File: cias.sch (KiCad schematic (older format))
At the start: 63 parts, among them CN13 KEYBOARD, CN6 SERIAL_DB25M, CN7 PARALLEL_DB25F, Q501 2N3904, Q502 2N3906, Q503 2N3906, Q711 2N3904, U38 MC1488, U39 MC1489, U42 NE555, U7 VIA_8520, U8 VIA_8520

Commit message: Add EMI filter types
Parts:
- E501, E502, E503: EMI_FILTER_TYPE (none) -> R
- E511, E512, E513, E514, E515, E516, E517, E518, E519, E521, E522, E523, E524, E631, E632: EMI_FILTER_TYPE (none) -> NORMAL
- E520, E531, E532, E533, E534, E535, E536, E537, E538: EMI_FILTER_TYPE (none) -> W/FERRITE
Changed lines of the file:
@@
 F 3 "http://www.murata.com/~/media/webrenewal/support/library/catalog/products/emc/emifil/c31e.ashx?la=en-gb" V 9950 1990 50  0001 C CNN
 F 4 "PARALLEL" H 9950 1990 50  0001 C CNN "Optional"
+F 5 "W/FERRITE" H 9950 1990 50  0001 C CNN "EMI_FILTER_TYPE"
 	1    9950 1990
 	-1   0    0    -1
@@
 F 3 "http://www.murata.com/~/media/webrenewal/support/library/catalog/products/emc/emifil/c31e.ashx?la=en-gb" V 8045 1490 50  0001 C CNN
 F 4 "PARALLEL" H 8045 1490 50  0001 C CNN "Optional"
+F 5 "NORMAL" H 8045 1490 50  0001 C CNN "EMI_FILTER_TYPE"
 	1    8045 1490
 	1    0    0    -1
@@
 F 3 "http://www.murata.com/~/media/webrenewal/support/library/catalog/products/emc/emifil/c31e.ashx?la=en-gb" V 8430 1690 50  0001 C CNN
 F 4 "PARALLEL" H 8430 1690 50  0001 C CNN "Optional"
+F 5 "NORMAL" H 8430 1690 50  0001 C CNN "EMI_FILTER_TYPE"
 	1    8430 1690
 	1    0    0    -1
@@
 F 3 "http://www.murata.com/~/media/webrenewal/support/library/catalog/products/emc/emifil/c31e.ashx?la=en-gb" V 8045 1890 50  0001 C CNN
 F 4 "PARALLEL" H 8045 1890 50  0001 C CNN "Optional"
+F 5 "NORMAL" H 8045 1890 50  0001 C CNN "EMI_FILTER_TYPE"
 	1    8045 1890
 	1    0    0    -1
@@
 F 3 "http://www.murata.com/~/media/webrenewal/support/library/catalog/products/emc/emifil/c31e.ashx?la=en-gb" V 8430 2090 50  0001 C CNN
 F 4 "PARALLEL" H 8430 2090 50  0001 C CNN "Optional"
+F 5 "NORMAL" H 8430 2090 50  0001 C CNN "EMI_FILTER_TYPE"
 	1    8430 2090
 	1    0    0    -1
@@
 F 3 "http://www.murata.com/~/media/webrenewal/support/library/catalog/products/emc/emifil/c31e.ashx?la=en-gb" V 8045 2290 50  0001 C CNN
 F 4 "PARALLEL" H 8045 2290 50  0001 C CNN "Optional"
+F 5 "NORMAL" H 8045 2290 50  0001 C CNN "EMI_FILTER_TYPE"
 	1    8045 2290
 	1    0    0    -1
@@
 F 3 "http://www.murata.com/~/media/webrenewal/support/library/catalog/products/emc/emifil/c31e.ashx?la=en-gb" V 8430 2490 50  0001 C CNN
 F 4 "PARALLEL" H 8430 2490 50  0001 C CNN "Optional"
+F 5 "NORMAL" H 8430 2490 50  0001 C CNN "EMI_FILTER_TYPE"
 	1    8430 2490
 	1    0    0    -1
@@
 F 3 "http://www.murata.com/~/media/webrenewal/support/library/catalog/products/emc/emifil/c31e.ashx?la=en-gb" V 8045 2690 50  0001 C CNN
 F 4 "PARALLEL" H 8045 2690 50  0001 C CNN "Optional"
+F 5 "NORMAL" H 8045 2690 50  0001 C CNN "EMI_FILTER_TYPE"
 	1    8045 2690
 	1    0    0    -1
@@
 F 3 "http://www.murata.com/~/media/webrenewal/support/library/catalog/products/emc/emifil/c31e.ashx?la=en-gb" V 8430 2890 50  0001 C CNN
 F 4 "PARALLEL" H 8430 2890 50  0001 C CNN "Optional"
+F 5 "NORMAL" H 8430 2890 50  0001 C CNN "EMI_FILTER_TYPE"
 	1    8430 2890
 	1    0    0    -1
@@
 F 3 "http://www.murata.com/~/media/webrenewal/support/library/catalog/products/emc/emifil/c31e.ashx?la=en-gb" V 8045 3090 50  0001 C CNN
 F 4 "PARALLEL" H 8045 3090 50  0001 C CNN "Optional"
+F 5 "NORMAL" H 8045 3090 50  0001 C CNN "EMI_FILTER_TYPE"
 	1    8045 3090
 	1    0    0    -1
@@
 F 3 "http://www.murata.com/~/media/webrenewal/support/library/catalog/products/emc/emifil/c31e.ashx?la=en-gb" V 8430 3290 50  0001 C CNN
 F 4 "PARALLEL" H 8430 3290 50  0001 C CNN "Optional"
+F 5 "NORMAL" H 8430 3290 50  0001 C CNN "EMI_FILTER_TYPE"
 	1    8430 3290
 	1    0    0    -1
@@
 F 3 "http://www.murata.com/~/media/webrenewal/support/library/catalog/products/emc/emifil/c31e.ashx?la=en-gb" V 8045 3490 50  0001 C CNN
 F 4 "PARALLEL" H 8045 3490 50  0001 C CNN "Optional"
+F 5 "NORMAL" H 8045 3490 50  0001 C CNN "EMI_FILTER_TYPE"
 	1    8045 3490
 	1    0    0    -1
@@
 F 3 "http://www.murata.com/~/media/webrenewal/support/library/catalog/products/emc/emifil/c31e.ashx?la=en-gb" V 8430 3690 50  0001 C CNN
 F 4 "PARALLEL" H 8430 3690 50  0001 C CNN "Optional"
+F 5 "NORMAL" H 8430 3690 50  0001 C CNN "EMI_FILTER_TYPE"
 	1    8430 3690
 	1    0    0    -1
@@
 F 3 "http://www.murata.com/~/media/webrenewal/support/library/catalog/products/emc/emifil/c31e.ashx?la=en-gb" V 8045 3890 50  0001 C CNN
 F 4 "PARALLEL" H 8045 3890 50  0001 C CNN "Optional"
+F 5 "NORMAL" H 8045 3890 50  0001 C CNN "EMI_FILTER_TYPE"
 	1    8045 3890
 	1    0    0    -1
@@
 F 3 "http://www.murata.com/~/media/webrenewal/support/library/catalog/products/emc/emifil/c31e.ashx?la=en-gb" V 8045 6710 50  0001 C CNN
 F 4 "SERIAL" H 8045 6710 50  0001 C CNN "Optional"
+F 5 "W/FERRITE" H 8045 6710 50  0001 C CNN "EMI_FILTER_TYPE"
 	1    8045 6710
 	1    0    0    -1
@@
 F 3 "http://www.murata.com/~/media/webrenewal/support/library/catalog/products/emc/emifil/c31e.ashx?la=en-gb" V 8430 6910 50  0001 C CNN
 F 4 "SERIAL" H 8430 6910 50  0001 C CNN "Optional"
+F 5 "W/FERRITE" H 8430 6910 50  0001 C CNN "EMI_FILTER_TYPE"
 	1    8430 6910
 	1    0    0    -1
@@
 F 3 "http://www.murata.com/~/media/webrenewal/support/library/catalog/products/emc/emifil/c31e.ashx?la=en-gb" V 8045 7110 50  0001 C CNN
 F 4 "SERIAL" H 8045 7110 50  0001 C CNN "Optional"
+F 5 "W/FERRITE" H 8045 7110 50  0001 C CNN "EMI_FILTER_TYPE"
 	1    8045 7110
 	1    0    0    -1
@@
 F 3 "http://www.murata.com/~/media/webrenewal/support/library/catalog/products/emc/emifil/c31e.ashx?la=en-gb" V 8430 7310 50  0001 C CNN
 F 4 "SERIAL" H 8430 7310 50  0001 C CNN "Optional"
+F 5 "W/FERRITE" H 8430 7310 50  0001 C CNN "EMI_FILTER_TYPE"
 	1    8430 7310
 	1    0    0    -1
@@
 F 3 "http://www.murata.com/~/media/webrenewal/support/library/catalog/products/emc/emifil/c31e.ashx?la=en-gb" V 8045 7910 50  0001 C CNN
 F 4 "SERIAL" H 8045 7910 50  0001 C CNN "Optional"
+F 5 "W/FERRITE" H 8045 7910 50  0001 C CNN "EMI_FILTER_TYPE"
 	1    8045 7910
 	1    0    0    -1
@@
 F 3 "http://www.murata.com/~/media/webrenewal/support/library/catalog/products/emc/emifil/c31e.ashx?la=en-gb" V 10180 7810 50  0001 C CNN
 F 4 "SERIAL" H 10180 7810 50  0001 C CNN "Optional"
+F 5 "W/FERRITE" H 10180 7810 50  0001 C CNN "EMI_FILTER_TYPE"
 	1    10180 7810
 	-1   0    0    -1
@@
 F 3 "http://www.murata.com/~/media/webrenewal/support/library/catalog/products/emc/emifil/c31e.ashx?la=en-gb" V 10180 8210 50  0001 C CNN
 F 4 "SERIAL" H 10180 8210 50  0001 C CNN "Optional"
+F 5 "W/FERRITE" H 10180 8210 50  0001 C CNN "EMI_FILTER_TYPE"
 	1    10180 8210
 	-1   0    0    -1
@@
 F 3 "http://www.murata.com/~/media/webrenewal/support/library/catalog/products/emc/emifil/c31e.ashx?la=en-gb" V 14545 4085 50  0001 C CNN
 F 4 "KEYBOARD" H 14545 4085 50  0001 C CNN "Optional"
+F 5 "NORMAL" H 14545 4085 50  0001 C CNN "EMI_FILTER_TYPE"
 	1    14545 4085
 	1    0    0    -1
@@
 F 3 "http://www.murata.com/~/media/webrenewal/support/library/catalog/products/emc/emifil/c31e.ashx?la=en-gb" V 14545 4440 50  0001 C CNN
 F 4 "KEYBOARD" H 14545 4440 50  0001 C CNN "Optional"
+F 5 "NORMAL" H 14545 4440 50  0001 C CNN "EMI_FILTER_TYPE"
 	1    14545 4440
 	1    0    0    -1
@@
 F 3 "http://www.murata.com/~/media/webrenewal/support/library/catalog/products/emc/emifil/c31e.ashx?la=en-gb" V 8045 7510 50  0001 C CNN
 F 4 "SERIAL" H 8045 7510 50  0001 C CNN "Optional"
+F 5 "W/FERRITE" H 8045 7510 50  0001 C CNN "EMI_FILTER_TYPE"
 	1    8045 7510
 	1    0    0    -1
@@
 F 3 "http://www.murata.com/~/media/webrenewal/support/library/catalog/products/emc/emifil/c31e.ashx?la=en-gb" V 8430 8110 50  0001 C CNN
 F 4 "SERIAL" H 8430 8110 50  0001 C CNN "Optional"
+F 5 "R" H 8430 8110 50  0001 C CNN "EMI_FILTER_TYPE"
 	1    8430 8110
 	1    0    0    -1
@@
 F 3 "http://www.murata.com/~/media/webrenewal/support/library/catalog/products/emc/emifil/c31e.ashx?la=en-gb" V 8045 8310 50  0001 C CNN
 F 4 "SERIAL" H 8045 8310 50  0001 C CNN "Optional"
+F 5 "R" H 8045 8310 50  0001 C CNN "EMI_FILTER_TYPE"
 	1    8045 8310
 	1    0    0    -1
@@
 F 3 "http://www.murata.com/~/media/webrenewal/support/library/catalog/products/emc/emifil/c31e.ashx?la=en-gb" V 10105 1590 50  0001 C CNN
 F 4 "PARALLEL" H 10105 1590 50  0001 C CNN "Optional"
+F 5 "R" H 10105 1590 50  0001 C CNN "EMI_FILTER_TYPE"
 	1    10105 1590
 	-1   0    0    -1

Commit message: Add part numbers for EMI filters Not the original filters, but what seem to be suitable replacements available today
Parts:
- E511, E512, E513, E514, E515, E516, E517, E518, E519, E521, E522, E523, E524, E631, E632: Cost (none) -> 0.233; MFG Part Num (none) -> DSS1NB32A101Q91A (has ferrite)
- E520, E531, E533, E535, E536, E537, E538: Cost (none) -> 0.233; MFG Name (none) -> MURATA; MFG Part Num (none) -> DSS1NB32A471Q91A
- E532, E534: Cost (none) -> 0.238; MFG Name (none) -> MURATA; MFG Part Num (none) -> DSS1NB32A151Q91A
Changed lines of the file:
@@
 F 4 "PARALLEL" H 9950 1990 50  0001 C CNN "Optional"
 F 5 "W/FERRITE" H 9950 1990 50  0001 C CNN "EMI_FILTER_TYPE"
+F 6 "0.233" H 9950 1990 50  0001 C CNN "Cost"
+F 7 "MURATA" H 9950 1990 50  0001 C CNN "MFG Name"
+F 8 "DSS1NB32A471Q91A" H 9950 1990 50  0001 C CNN "MFG Part Num"
 	1    9950 1990
 	-1   0    0    -1
@@
 F 4 "PARALLEL" H 8045 1490 50  0001 C CNN "Optional"
 F 5 "NORMAL" H 8045 1490 50  0001 C CNN "EMI_FILTER_TYPE"
+F 6 "0.233" H 8045 1490 50  0001 C CNN "Cost"
+F 7 "DSS1NB32A101Q91A (has ferrite)" H 8045 1490 50  0001 C CNN "MFG Part Num"
 	1    8045 1490
 	1    0    0    -1
@@
 F 4 "PARALLEL" H 8430 1690 50  0001 C CNN "Optional"
 F 5 "NORMAL" H 8430 1690 50  0001 C CNN "EMI_FILTER_TYPE"
+F 6 "0.233" H 8430 1690 50  0001 C CNN "Cost"
+F 7 "DSS1NB32A101Q91A (has ferrite)" H 8430 1690 50  0001 C CNN "MFG Part Num"
 	1    8430 1690
 	1    0    0    -1
@@
 F 4 "PARALLEL" H 8045 1890 50  0001 C CNN "Optional"
 F 5 "NORMAL" H 8045 1890 50  0001 C CNN "EMI_FILTER_TYPE"
+F 6 "0.233" H 8045 1890 50  0001 C CNN "Cost"
+F 7 "DSS1NB32A101Q91A (has ferrite)" H 8045 1890 50  0001 C CNN "MFG Part Num"
 	1    8045 1890
 	1    0    0    -1
@@
 F 4 "PARALLEL" H 8430 2090 50  0001 C CNN "Optional"
 F 5 "NORMAL" H 8430 2090 50  0001 C CNN "EMI_FILTER_TYPE"
+F 6 "0.233" H 8430 2090 50  0001 C CNN "Cost"
+F 7 "DSS1NB32A101Q91A (has ferrite)" H 8430 2090 50  0001 C CNN "MFG Part Num"
 	1    8430 2090
 	1    0    0    -1
@@
 F 4 "PARALLEL" H 8045 2290 50  0001 C CNN "Optional"
 F 5 "NORMAL" H 8045 2290 50  0001 C CNN "EMI_FILTER_TYPE"
+F 6 "0.233" H 8045 2290 50  0001 C CNN "Cost"
+F 7 "DSS1NB32A101Q91A (has ferrite)" H 8045 2290 50  0001 C CNN "MFG Part Num"
 	1    8045 2290
 	1    0    0    -1
@@
 F 4 "PARALLEL" H 8430 2490 50  0001 C CNN "Optional"
 F 5 "NORMAL" H 8430 2490 50  0001 C CNN "EMI_FILTER_TYPE"
+F 6 "0.233" H 8430 2490 50  0001 C CNN "Cost"
+F 7 "DSS1NB32A101Q91A (has ferrite)" H 8430 2490 50  0001 C CNN "MFG Part Num"
 	1    8430 2490
 	1    0    0    -1
@@
 F 4 "PARALLEL" H 8045 2690 50  0001 C CNN "Optional"
 F 5 "NORMAL" H 8045 2690 50  0001 C CNN "EMI_FILTER_TYPE"
+F 6 "0.233" H 8045 2690 50  0001 C CNN "Cost"
+F 7 "DSS1NB32A101Q91A (has ferrite)" H 8045 2690 50  0001 C CNN "MFG Part Num"
 	1    8045 2690
 	1    0    0    -1
@@
 F 4 "PARALLEL" H 8430 2890 50  0001 C CNN "Optional"
 F 5 "NORMAL" H 8430 2890 50  0001 C CNN "EMI_FILTER_TYPE"
+F 6 "0.233" H 8430 2890 50  0001 C CNN "Cost"
+F 7 "DSS1NB32A101Q91A (has ferrite)" H 8430 2890 50  0001 C CNN "MFG Part Num"
 	1    8430 2890
 	1    0    0    -1
@@
 F 4 "PARALLEL" H 8045 3090 50  0001 C CNN "Optional"
 F 5 "NORMAL" H 8045 3090 50  0001 C CNN "EMI_FILTER_TYPE"
+F 6 "0.233" H 8045 3090 50  0001 C CNN "Cost"
+F 7 "DSS1NB32A101Q91A (has ferrite)" H 8045 3090 50  0001 C CNN "MFG Part Num"
 	1    8045 3090
 	1    0    0    -1
@@
 F 4 "PARALLEL" H 8430 3290 50  0001 C CNN "Optional"
 F 5 "NORMAL" H 8430 3290 50  0001 C CNN "EMI_FILTER_TYPE"
+F 6 "0.233" H 8430 3290 50  0001 C CNN "Cost"
+F 7 "DSS1NB32A101Q91A (has ferrite)" H 8430 3290 50  0001 C CNN "MFG Part Num"
 	1    8430 3290
 	1    0    0    -1
@@
 F 4 "PARALLEL" H 8045 3490 50  0001 C CNN "Optional"
 F 5 "NORMAL" H 8045 3490 50  0001 C CNN "EMI_FILTER_TYPE"
+F 6 "0.233" H 8045 3490 50  0001 C CNN "Cost"
+F 7 "DSS1NB32A101Q91A (has ferrite)" H 8045 3490 50  0001 C CNN "MFG Part Num"
 	1    8045 3490
 	1    0    0    -1
@@
 F 4 "PARALLEL" H 8430 3690 50  0001 C CNN "Optional"
 F 5 "NORMAL" H 8430 3690 50  0001 C CNN "EMI_FILTER_TYPE"
+F 6 "0.233" H 8430 3690 50  0001 C CNN "Cost"
+F 7 "DSS1NB32A101Q91A (has ferrite)" H 8430 3690 50  0001 C CNN "MFG Part Num"
 	1    8430 3690
 	1    0    0    -1
@@
 F 4 "PARALLEL" H 8045 3890 50  0001 C CNN "Optional"
 F 5 "NORMAL" H 8045 3890 50  0001 C CNN "EMI_FILTER_TYPE"
+F 6 "0.233" H 8045 3890 50  0001 C CNN "Cost"
+F 7 "DSS1NB32A101Q91A (has ferrite)" H 8045 3890 50  0001 C CNN "MFG Part Num"
 	1    8045 3890
 	1    0    0    -1
@@
 F 4 "SERIAL" H 8045 6710 50  0001 C CNN "Optional"
 F 5 "W/FERRITE" H 8045 6710 50  0001 C CNN "EMI_FILTER_TYPE"
+F 6 "0.238" H 8045 6710 50  0001 C CNN "Cost"
+F 7 "MURATA" H 8045 6710 50  0001 C CNN "MFG Name"
+F 8 "DSS1NB32A151Q91A " H 8045 6710 50  0001 C CNN "MFG Part Num"
 	1    8045 6710
 	1    0    0    -1
@@
 F 4 "SERIAL" H 8430 6910 50  0001 C CNN "Optional"
 F 5 "W/FERRITE" H 8430 6910 50  0001 C CNN "EMI_FILTER_TYPE"
+F 6 "0.238" H 8430 6910 50  0001 C CNN "Cost"
+F 7 "MURATA" H 8430 6910 50  0001 C CNN "MFG Name"
+F 8 "DSS1NB32A151Q91A " H 8430 6910 50  0001 C CNN "MFG Part Num"
 	1    8430 6910
 	1    0    0    -1
@@
 F 4 "SERIAL" H 8045 7110 50  0001 C CNN "Optional"
 F 5 "W/FERRITE" H 8045 7110 50  0001 C CNN "EMI_FILTER_TYPE"
+F 6 "0.233" H 8045 7110 50  0001 C CNN "Cost"
+F 7 "MURATA" H 8045 7110 50  0001 C CNN "MFG Name"
+F 8 "DSS1NB32A471Q91A" H 8045 7110 50  0001 C CNN "MFG Part Num"
 	1    8045 7110
 	1    0    0    -1
@@
 F 4 "SERIAL" H 8430 7310 50  0001 C CNN "Optional"
 F 5 "W/FERRITE" H 8430 7310 50  0001 C CNN "EMI_FILTER_TYPE"
+F 6 "0.233" H 8430 7310 50  0001 C CNN "Cost"
+F 7 "MURATA" H 8430 7310 50  0001 C CNN "MFG Name"
+F 8 "DSS1NB32A471Q91A" H 8430 7310 50  0001 C CNN "MFG Part Num"
 	1    8430 7310
 	1    0    0    -1
@@
 F 4 "SERIAL" H 8045 7910 50  0001 C CNN "Optional"
 F 5 "W/FERRITE" H 8045 7910 50  0001 C CNN "EMI_FILTER_TYPE"
+F 6 "0.233" H 8045 7910 50  0001 C CNN "Cost"
+F 7 "MURATA" H 8045 7910 50  0001 C CNN "MFG Name"
+F 8 "DSS1NB32A471Q91A" H 8045 7910 50  0001 C CNN "MFG Part Num"
 	1    8045 7910
 	1    0    0    -1
@@
 F 4 "SERIAL" H 10180 7810 50  0001 C CNN "Optional"
 F 5 "W/FERRITE" H 10180 7810 50  0001 C CNN "EMI_FILTER_TYPE"
+F 6 "0.233" H 10180 7810 50  0001 C CNN "Cost"
+F 7 "MURATA" H 10180 7810 50  0001 C CNN "MFG Name"
+F 8 "DSS1NB32A471Q91A" H 10180 7810 50  0001 C CNN "MFG Part Num"
 	1    10180 7810
 	-1   0    0    -1
@@
 F 4 "SERIAL" H 10180 8210 50  0001 C CNN "Optional"
 F 5 "W/FERRITE" H 10180 8210 50  0001 C CNN "EMI_FILTER_TYPE"
+F 6 "0.233" H 10180 8210 50  0001 C CNN "Cost"
+F 7 "MURATA" H 10180 8210 50  0001 C CNN "MFG Name"
+F 8 "DSS1NB32A471Q91A" H 10180 8210 50  0001 C CNN "MFG Part Num"
 	1    10180 8210
 	-1   0    0    -1
@@
 F 4 "KEYBOARD" H 14545 4085 50  0001 C CNN "Optional"
 F 5 "NORMAL" H 14545 4085 50  0001 C CNN "EMI_FILTER_TYPE"
+F 6 "0.233" H 14545 4085 50  0001 C CNN "Cost"
+F 7 "DSS1NB32A101Q91A (has ferrite)" H 14545 4085 50  0001 C CNN "MFG Part Num"
 	1    14545 4085
 	1    0    0    -1
@@
 F 4 "KEYBOARD" H 14545 4440 50  0001 C CNN "Optional"
 F 5 "NORMAL" H 14545 4440 50  0001 C CNN "EMI_FILTER_TYPE"
+F 6 "0.233" H 14545 4440 50  0001 C CNN "Cost"
+F 7 "DSS1NB32A101Q91A (has ferrite)" H 14545 4440 50  0001 C CNN "MFG Part Num"
 	1    14545 4440
 	1    0    0    -1
@@
 F 4 "SERIAL" H 8045 7510 50  0001 C CNN "Optional"
 F 5 "W/FERRITE" H 8045 7510 50  0001 C CNN "EMI_FILTER_TYPE"
+F 6 "0.233" H 8045 7510 50  0001 C CNN "Cost"
+F 7 "MURATA" H 8045 7510 50  0001 C CNN "MFG Name"
+F 8 "DSS1NB32A471Q91A" H 8045 7510 50  0001 C CNN "MFG Part Num"
 	1    8045 7510
 	1    0    0    -1

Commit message: Make C712 footprint smaller
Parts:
- C712: footprint Capacitor_THT:CP_Radial_D8.0mm_P5.00mm -> Capacitor_THT:CP_Radial_D5.0mm_P2.50mm
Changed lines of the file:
@@
 F 0 "C712" H 12105 7841 50  0000 L CNN
 F 1 "10u" H 12105 7750 50  0000 L CNN
-F 2 "Capacitor_THT:CP_Radial_D8.0mm_P5.00mm" H 11990 7795 50  0001 C CNN
+F 2 "Capacitor_THT:CP_Radial_D5.0mm_P2.50mm" H 11990 7795 50  0001 C CNN
 F 3 "~" H 11990 7795 50  0001 C CNN
 F 4 "POR" H 11990 7795 50  0001 C CNN "Optional"

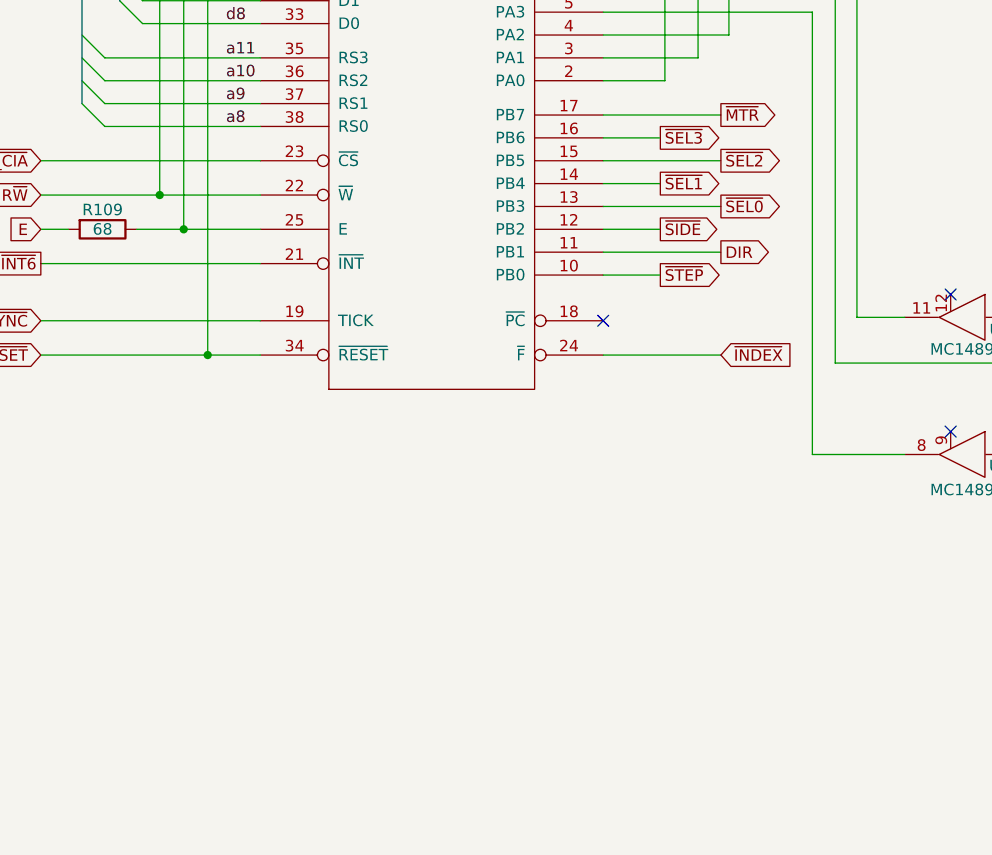
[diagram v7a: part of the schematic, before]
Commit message: Add drive switcher
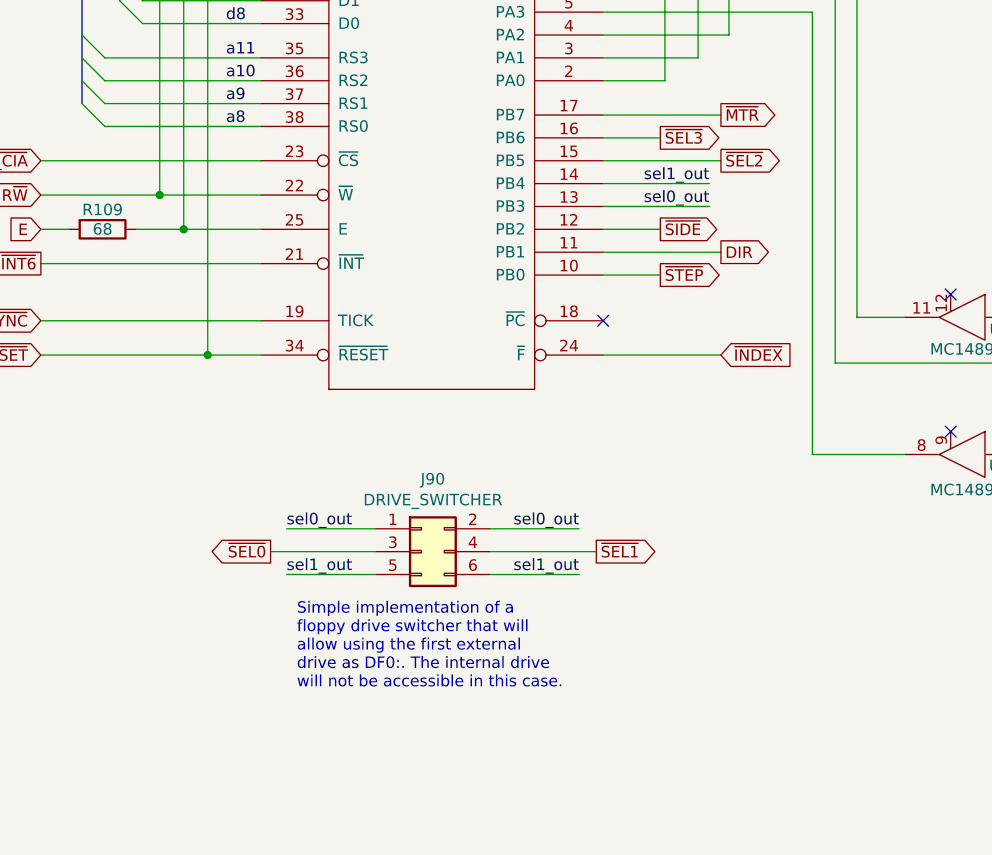
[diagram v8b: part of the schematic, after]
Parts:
- added J90: DRIVE_SWITCHER, Raemixx500:DriveSwitchHeader, symbol Connector_Generic:Conn_02x03_Odd_Even
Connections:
- net ~SEL0: now also J90.3 (Pin_3); no longer U8.13 (PB3)
- net ~SEL1: now also J90.4 (Pin_4); no longer U8.14 (PB4)
- new net sel0_out: J90.1 (Pin_1), J90.2 (Pin_2), U8.13 (PB3)
- new net sel1_out: J90.5 (Pin_5), J90.6 (Pin_6), U8.14 (PB4)
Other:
- note added: "Simple implementation of a\nfloppy drive switcher that will\nallow using the first external\ndrive as DF0:. The internal drive\nwill not be accessible in this case."
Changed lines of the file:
@@
 	4065 6525 4580 6525
-Wire Wire Line
-	4065 6625 4315 6625
-Wire Wire Line
-	4065 6725 4580 6725
 Wire Wire Line
 	4065 6825 4315 6825
@@
 Text GLabel 4580 6525 2    50   Output ~ 0
 ~SEL2
-Text GLabel 4315 6625 2    50   Output ~ 0
-~SEL1
-Text GLabel 4580 6725 2    50   Output ~ 0
-~SEL0
 Text GLabel 4315 6825 2    50   Output ~ 0
 ~SIDE
@@
 	1    0    0    -1
 $EndComp
+Text GLabel 2610 8235 0    50   Output ~ 0
+~SEL0
+Text GLabel 4035 8235 2    50   Output ~ 0
+~SEL1
+Wire Wire Line
+	4065 6625 4530 6625
+Wire Wire Line
+	4065 6725 4530 6725
+Text Label 4530 6725 2    50   ~ 0
+sel0_out
+Text Label 4530 6625 2    50   ~ 0
+sel1_out
+Text Label 2680 8135 0    50   ~ 0
+sel0_out
+Wire Wire Line
+	3070 8335 2680 8335
+Text Label 2680 8335 0    50   ~ 0
+sel1_out
+Text Label 3960 8135 2    50   ~ 0
+sel0_out
+Wire Wire Line
+	3960 8135 3570 8135
+Text Label 3960 8335 2    50   ~ 0
+sel1_out
+Text Notes 2725 8840 0    50   ~ 0
+Simple implementation of a\nfloppy drive switcher that will\nallow using the first external\ndrive as DF0:. The internal drive\nwill not be accessible in this case.
+$Comp
+L Connector_Generic:Conn_02x03_Odd_Even J90
+U 1 1 5EFAA487
+P 3270 8235
+F 0 "J90" H 3320 8552 50  0000 C CNN
+F 1 "DRIVE_SWITCHER" H 3320 8461 50  0000 C CNN
+F 2 "Raemixx500:DriveSwitchHeader" H 3270 8235 50  0001 C CNN
+F 3 "~" H 3270 8235 50  0001 C CNN
+	1    3270 8235
+	1    0    0    -1
+$EndComp
+Wire Wire Line
+	2680 8135 3070 8135
+Wire Wire Line
+	2610 8235 3070 8235
+Wire Wire Line
+	3570 8235 4035 8235
+Wire Wire Line
+	3570 8335 3960 8335
 Wire Bus Line
 	1785 3110 1785 6275
